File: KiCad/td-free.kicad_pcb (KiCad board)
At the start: 2 copper layers, 60 x 30 mm, 6 parts, among them J1 Conn_01x02_Pin, Q1 2N7002, U1 ESP32-C3_SUPERMINI, U2 VEML7700-TT

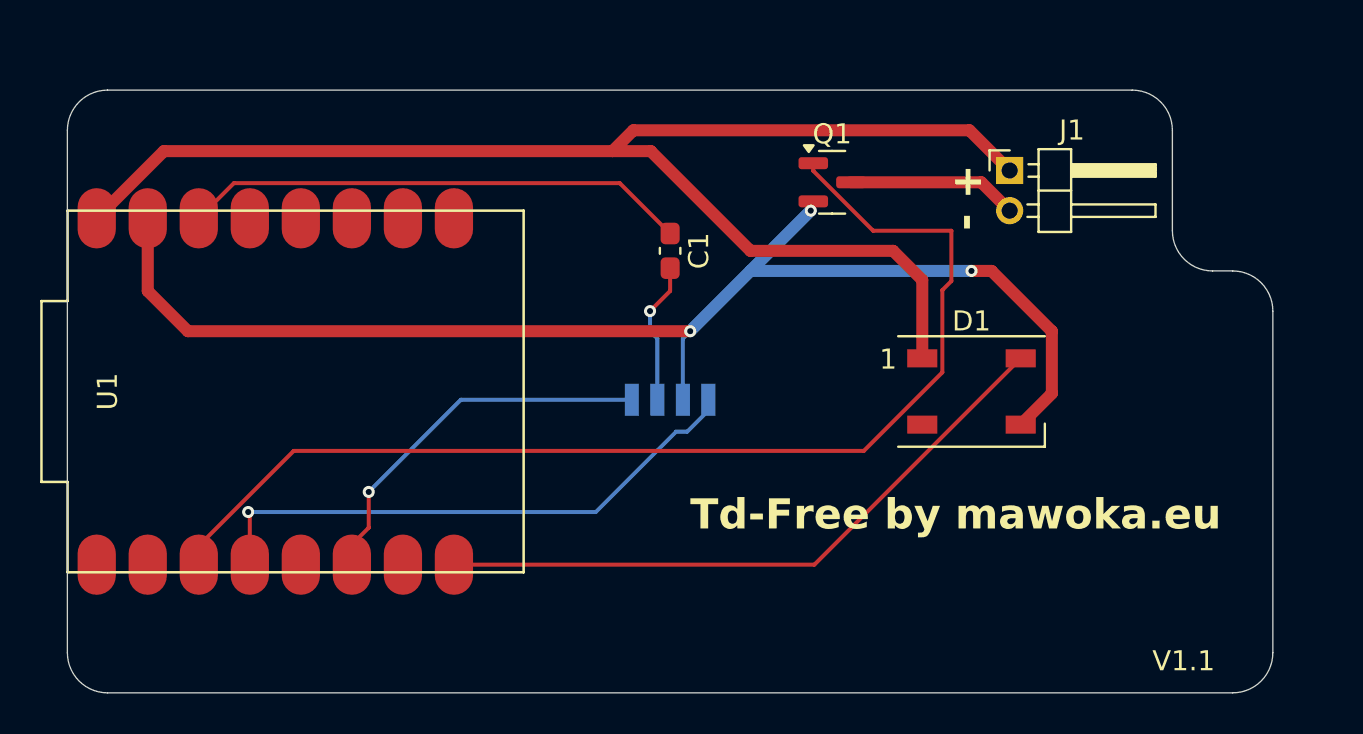
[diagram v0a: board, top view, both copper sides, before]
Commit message: Add V1.2 PCB without wrong condensator
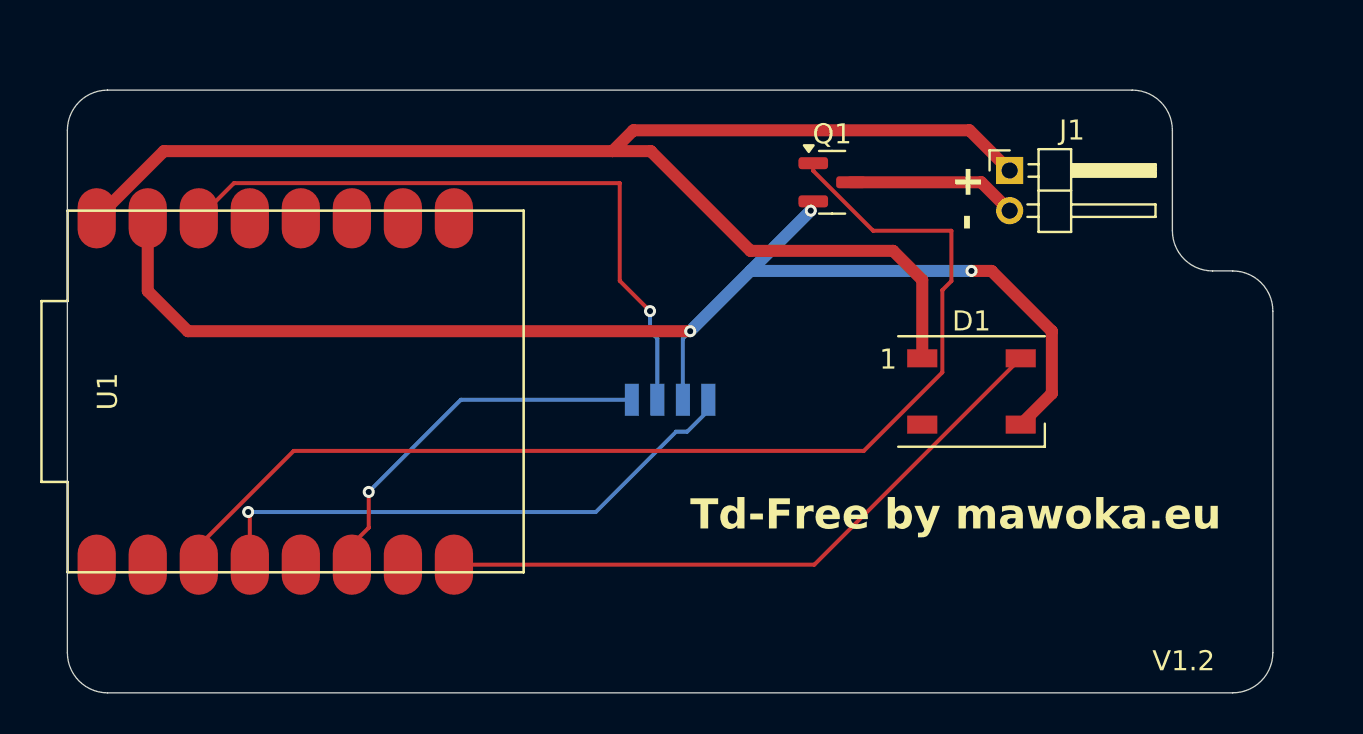
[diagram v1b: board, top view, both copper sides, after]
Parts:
- removed C1: C_Small, Capacitor_SMD:C_0603_1608Metric_Pad1.08x0.95mm_HandSolder
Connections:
- U2 pad 2: Net-(U2-VDD) -> Net-(U1-3V3)
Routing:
- net Net-(U1-3V3): track 25.2 -> 32.7 mm, vias 0 -> 1
- net Net-(U2-VDD): track 6.62 -> 0.00 mm, vias 1 -> 0
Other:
- board text added: "V1.2"
- board text removed: "V1.1"

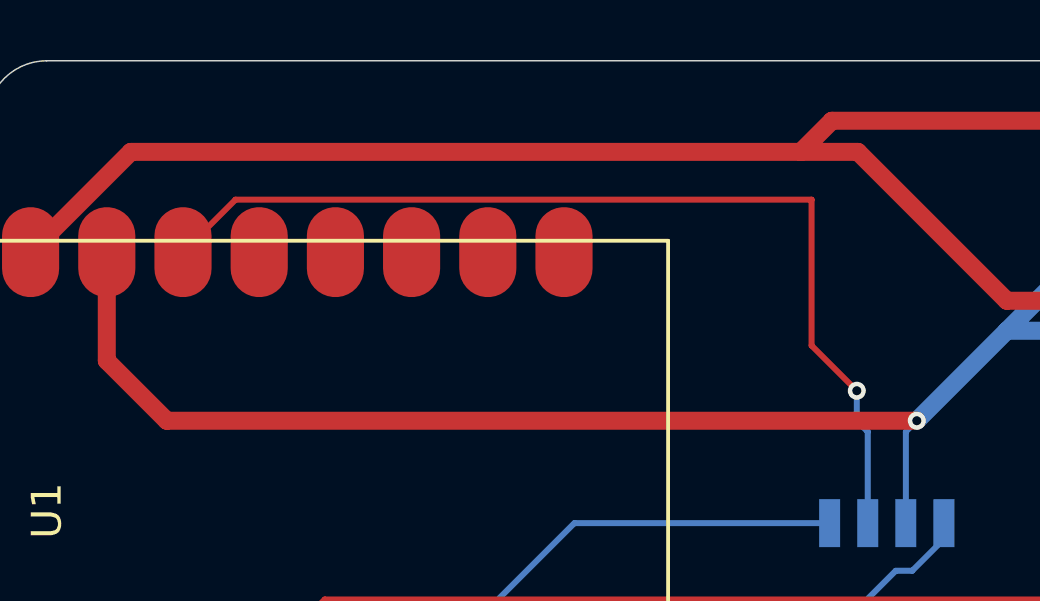
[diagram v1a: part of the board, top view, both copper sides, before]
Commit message: Optimize trace on PCB
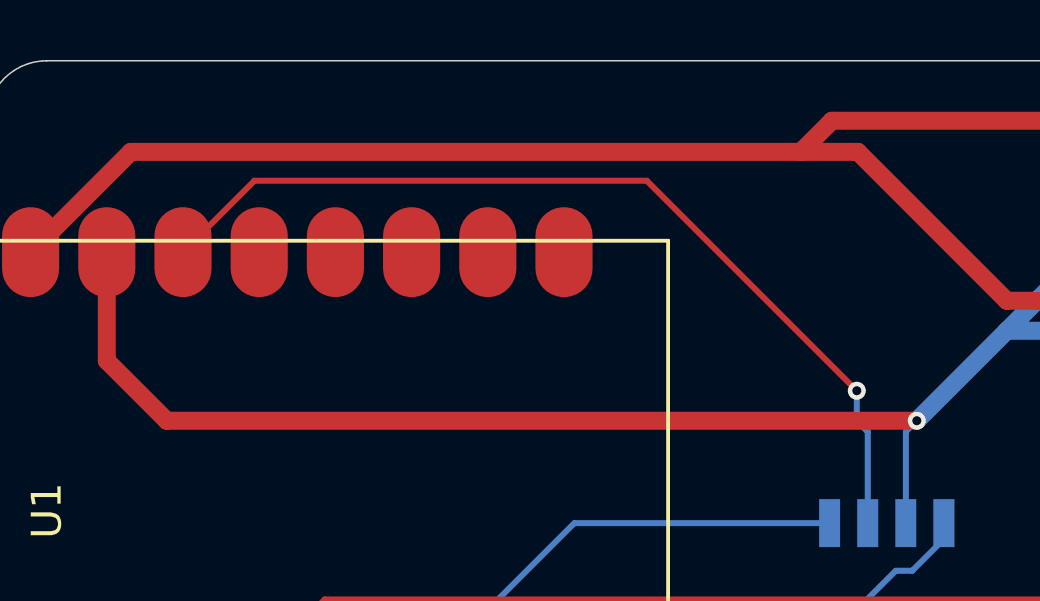
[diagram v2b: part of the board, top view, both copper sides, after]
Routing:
- net Net-(U1-3V3): track 32.7 -> 30.4 mm
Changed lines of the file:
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@@
 	)
 	(segment
-		(start 41.4925 19.63)
-		(end 41.4925 24.4925)
+		(start 22.92 19)
+		(end 20.54 21.38)
 		(width 0.2)
 		(layer "F.Cu")
@@
 	)
 	(segment
-		(start 22.29 19.63)
-		(end 41.4925 19.63)
+		(start 43 26)
+		(end 36 19)
 		(width 0.2)
 		(layer "F.Cu")
@@
 	)
 	(segment
-		(start 41.4925 24.4925)
-		(end 43 26)
+		(start 36 19)
+		(end 22.92 19)
 		(width 0.2)
 		(layer "F.Cu")
-		(net 5)
-	)
-	(segment
-		(start 20.54 21.38)
-		(end 22.29 19.63)
-		(width 0.2)
-		(layer "F.Cu")

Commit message: :sparkles: First Prototype for improved PCB
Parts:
- added C1: 10uF, Capacitor_SMD:C_0805_2012Metric_Pad1.18x1.45mm_HandSolder, F.Cu at (21.0, 19.0)
- added C2: 22uF, Capacitor_SMD:C_0805_2012Metric_Pad1.18x1.45mm_HandSolder, F.Cu at (37.0, 19.0)
- added C3: 22uF, Capacitor_SMD:C_0805_2012Metric_Pad1.18x1.45mm_HandSolder, F.Cu at (38.0, 26.0)
- added C4: 10uF, Capacitor_SMD:C_0805_2012Metric_Pad1.18x1.45mm_HandSolder, F.Cu at (48.0, 28.0)
- added C5: 0.1uF, Capacitor_SMD:C_0805_2012Metric_Pad1.18x1.45mm_HandSolder, F.Cu at (48.0, 24.0)
- added C6: 10uF, Capacitor_SMD:C_0805_2012Metric_Pad1.18x1.45mm_HandSolder, F.Cu at (38.0, 31.0)
- added D2: SMAJ5.0A, Diode_SMD:D_SMA, F.Cu at (19.0, 38.0)
- added J2: USB_C_Receptacle_USB2.0_14P, Connector_USB:USB_C_Receptacle_GCT_USB4105-xx-A_16P_TopMnt_Horizontal, F.Cu at (18.2, 30.0)
- added R1: 5k1, Resistor_SMD:R_0805_2012Metric_Pad1.20x1.40mm_HandSolder, F.Cu at (22.0, 22.0)
- added R2: 5k1, Resistor_SMD:R_0805_2012Metric_Pad1.20x1.40mm_HandSolder, F.Cu at (18.0, 22.0)
- added R3: 10kO, Resistor_SMD:R_0805_2012Metric_Pad1.20x1.40mm_HandSolder, F.Cu at (50.0, 40.0)
- added U3: AMS1117-3.3, Package_TO_SOT_SMD:SOT-223-3_TabPin2, F.Cu at (29.1, 20.7)
- added U4: VEML3328, footprints:SMD_L3328_VIS, F.Cu at (44.0, 32.7)
- added U5: TPD4E05U06DQA, Package_SON:USON-10_2.5x1.0mm_P0.5mm, F.Cu at (25.4, 35.0)
- J1: footprint Connector_PinHeader_2.00mm:PinHeader_1x02_P2.00mm_Horizontal -> Connector_PinHeader_2.54mm:PinHeader_1x02_P2.54mm_Vertical
- U1: value ESP32-C3_SUPERMINI -> ESP32-C3-WROOM-02; footprint ESP32-C3_SUPERMINI:MODULE_ESP32-C3_SUPERMINI -> PCM_Espressif:ESP32-C3-WROOM-02
- U2: footprint VEML7700-TT:XDCR_VEML7700-TT -> VEML7700_TR:XDCR_VEML7700-TR; moved to F.Cu
- moved U1 33.6 mm to (58.9, 28.3), turned to 0 degrees
- moved D1 28.0 mm to (31.0, 30.0)
- moved Q1 21.8 mm to (55.9, 41.0)
- moved J1 12.9 mm to (71.0, 27.0)
- moved U2 5.32 mm to (44.3, 26.0), turned to 0 degrees
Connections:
- net Net-(U1-GPIO10) renamed /SCL
- D1 pad 1: Net-(D1-VDD) -> VBUS
- D1 pad 3: Net-(D1-VSS) -> GND
- D1 pad 4: Net-(D1-DIN) -> /RGB_DATA
- J1 pad 1: Net-(D1-VDD) -> VBUS
- Q1 pad 1: Net-(Q1-G) -> /LED_C
- Q1 pad 2: Net-(D1-VSS) -> GND
- U1 pad 1: unconnected-(U1-GPIO1-Pad1) -> +3V3
- U1 pad 2: unconnected-(U1-GPIO2-Pad2) -> Net-(U1-EN/CHIP_PU)
- U1 pad 6: unconnected-(U1-GPIO6-Pad6) -> /LED_C
- U1 pad 7: Net-(Q1-G) -> /SDA
- U1 pad 8: Net-(U1-GPIO8) -> /RGB_DATA
- U1 pad 9: unconnected-(U1-GPIO9-Pad9) -> GND
- U2 pad 2: Net-(U1-3V3) -> +3V3
- U2 pad 3: Net-(D1-VSS) -> GND
- U2 pad 4: Net-(U1-GPIO8) -> /SDA
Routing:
- net VBUS: track 0.00 -> 108.5 mm
- net Net-(D1-VDD): track 70.1 -> 0.00 mm
- net Net-(D1-VSS): track 64.0 -> 0.00 mm, vias 3 -> 0
- net /USB_D+: track 0.00 -> 57.9 mm, vias 0 -> 2
- net Net-(Q1-G): track 57.3 -> 0.00 mm
- net +3V3: track 0.00 -> 55.8 mm
- net /USB_D-: track 0.00 -> 55.8 mm, vias 0 -> 3
- net Net-(D1-DIN): track 32.5 -> 0.00 mm
- net Net-(U1-3V3): track 30.4 -> 0.00 mm, vias 1 -> 0
- net Net-(U1-GPIO8): track 27.2 -> 0.00 mm, vias 1 -> 0
- net GND: track 0.00 -> 24.8 mm, vias 0 -> 30
- net /RGB_DATA: track 0.00 -> 18.8 mm, vias 0 -> 2
- net /SCL: track 18.0 -> 36.6 mm, vias 1 -> 3
- net Net-(U1-EN/CHIP_PU): track 0.00 -> 18.3 mm
- net Net-(J1-Pin_2): track 8.49 -> 21.4 mm
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- added copper zone on B.Cu, net GND
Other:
- outline, holes or cut-outs redrawn
- board text added: "V2.0"
- board text removed: "- +"
- board text removed: "V1.2"

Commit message: :sparkles: First test with new PCB
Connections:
- U1 pad 10: /SCL -> /SCL1
- U1 pad 4: unconnected-(U1-GPIO5/ADC2_CH0-Pad4) -> /SCL2
- U1 pad 5: unconnected-(U1-GPIO6-Pad5) -> /SDA2
- U1 pad 7: /SDA -> /SDA1
- U2 pad 1: /SCL -> /SCL2
- U2 pad 4: /SDA -> /SDA2
- U4 pad 2: /SDA -> /SDA1
- U4 pad 3: /SCL -> /SCL1
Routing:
- net /SCL: track 36.6 -> 0.00 mm, vias 3 -> 0
- net /SCL1: track 0.00 -> 24.2 mm, vias 0 -> 2
- net /SDA: track 12.0 -> 0.00 mm, vias 2 -> 0
- net /SDA1: track 0.00 -> 7.86 mm, vias 0 -> 2
- net /SCL2: track 0.00 -> 6.39 mm, vias 0 -> 2
- net /SDA2: track 0.00 -> 5.40 mm
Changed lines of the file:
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@@
 	(title_block
 		(title "Td-Free")
-		(rev "0")
+		(rev "1")
 		(comment 4 "AISLER Project ID: AKNQHGTF")
 	)
@@
 	(net 13 "unconnected-(U1-GPIO20{slash}U0RXD-Pad11)")
 	(net 14 "unconnected-(U1-GPIO2{slash}ADC1_CH2-Pad16)")
-	(net 15 "unconnected-(U1-GPIO5{slash}ADC2_CH0-Pad4)")
+	(net 15 "/SCL2")
 	(net 16 "unconnected-(U1-GPIO0{slash}ADC1_CH0{slash}XTAL_32K_P-Pad18)")
 	(net 17 "unconnected-(U1-GPIO4{slash}ADC1_CH4-Pad3)")
 	(net 18 "unconnected-(U1-GPIO1{slash}ADC1_CH1{slash}XTAL_32K_N-Pad17)")
 	(net 19 "unconnected-(U1-GPIO3{slash}ADC1_CH3-Pad15)")
-	(net 20 "unconnected-(U1-GPIO6-Pad5)")
+	(net 20 "/SDA2")
 	(net 21 "unconnected-(U1-GPIO21{slash}U0TXD-Pad12)")
-	(net 22 "/SCL")
-	(net 23 "/SDA")
+	(net 22 "/SCL1")
+	(net 23 "/SDA1")
 	(net 24 "unconnected-(U5-NC-Pad10)")
 	(net 25 "unconnected-(U5-NC-Pad6)")
@@
 			(size 1.5 0.9)
 			(layers "F.Cu" "F.Mask" "F.Paste")
-			(net 15 "unconnected-(U1-GPIO5{slash}ADC2_CH0-Pad4)")
+			(net 15 "/SCL2")
 			(pinfunction "GPIO5/ADC2_CH0")
-			(pintype "bidirectional+no_connect")
+			(pintype "bidirectional")
 		)
 		(pad "5" smd rect
@@
 			(size 1.5 0.9)
 			(layers "F.Cu" "F.Mask" "F.Paste")
-			(net 20 "unconnected-(U1-GPIO6-Pad5)")
+			(net 20 "/SDA2")
 			(pinfunction "GPIO6")
-			(pintype "bidirectional+no_connect")
+			(pintype "bidirectional")
 		)
 		(pad "6" smd rect
@@
 			(size 1.5 0.9)
 			(layers "F.Cu" "F.Mask" "F.Paste")
-			(net 23 "/SDA")
+			(net 23 "/SDA1")
 			(pinfunction "GPIO8")
 			(pintype "bidirectional")
@@
 			(size 1.5 0.9)
 			(layers "F.Cu" "F.Mask" "F.Paste")
-			(net 22 "/SCL")
+			(net 22 "/SCL1")
 			(pinfunction "GPIO10")
 			(pintype "bidirectional")
@@
 			(size 1.4 0.7)
 			(layers "F.Cu" "F.Mask" "F.Paste")
-			(net 22 "/SCL")
+			(net 15 "/SCL2")
 			(pinfunction "SCL")
 			(pintype "input")
@@
 			(size 1.4 0.7)
 			(layers "F.Cu" "F.Mask" "F.Paste")
-			(net 23 "/SDA")
+			(net 20 "/SDA2")
 			(pinfunction "SDA")
 			(pintype "bidirectional")
@@
 			(size 0.4318 0.3048)
 			(layers "F.Cu" "F.Mask" "F.Paste")
-			(net 23 "/SDA")
+			(net 23 "/SDA1")
 			(pinfunction "SDA")
 			(pintype "bidirectional")
@@
 			(size 0.5334 0.3556)
 			(layers "F.Cu" "F.Mask" "F.Paste")
-			(net 22 "/SCL")
+			(net 22 "/SCL1")
 			(pinfunction "SCL")
 			(pintype "input")
@@
 	)
 	(segment
-		(start 52.4 34.4)
-		(end 67.69 34.4)
+		(start 45.881838 24.095)
+		(end 45.988419 23.988419)
 		(width 0.2)
 		(layer "F.Cu")
-		(net 22)
+		(net 15)
 	)
 	(segment
@@
 		(width 0.2)
 		(layer "F.Cu")
+		(net 15)
+	)
+	(segment
+		(start 45 24.095)
+		(end 45.881838 24.095)
+		(width 0.2)
+		(layer "F.Cu")
+		(net 15)
+	)
+	(via
+		(at 50 27)
+		(size 0.6)
+		(drill 0.3)
+		(layers "F.Cu" "B.Cu")
+		(net 15)
+	)
+	(via
+		(at 45.988419 23.988419)
+		(size 0.6)
+		(drill 0.3)
+		(layers "F.Cu" "B.Cu")
+		(net 15)
+	)
+	(segment
+		(start 45.988419 23.988419)
+		(end 49 27)
+		(width 0.2)
+		(layer "B.Cu")
+		(net 15)
+	)
+	(segment
+		(start 49 27)
+		(end 50 27)
+		(width 0.2)
+		(layer "B.Cu")
+		(net 15)
+	)
+	(segment
+		(start 49.695 27.905)
+		(end 50.19 28.4)
+		(width 0.2)
+		(layer "F.Cu")
+		(net 20)
+	)
+	(segment
+		(start 45 27.905)
+		(end 49.695 27.905)
+		(width 0.2)
+		(layer "F.Cu")
+		(net 20)
+	)
+	(segment
+		(start 52.4 34.4)
+		(end 67.69 34.4)
+		(width 0.2)
+		(layer "F.Cu")
 		(net 22)
 	)
@@
 	)
 	(via
-		(at 45 24)
-		(size 0.6)
-		(drill 0.3)
-		(layers "F.Cu" "B.Cu")
-		(net 22)
-	)
-	(via
 		(at 52 34)
 		(size 0.6)
@@
 	)
 	(segment
-		(start 45 34)
-		(end 48.5 30.5)
-		(width 0.2)
-		(layer "B.Cu")
-		(net 22)
-	)
-	(segment
-		(start 48 30)
-		(end 48.5 30.5)
-		(width 0.2)
-		(layer "B.Cu")
-		(net 22)
-	)
-	(segment
-		(start 48.5 30.5)
-		(end 52 34)
+		(start 45.361 33.639)
+		(end 45 34)
 		(width 0.2)
 		(layer "B.Cu")
@@
 	)
 	(segment
-		(start 45 30)
-		(end 48 30)
+		(start 52 34)
+		(end 51.639 33.639)
 		(width 0.2)
 		(layer "B.Cu")
@@
 	)
 	(segment
-		(start 45 24)
-		(end 45 30)
+		(start 51.639 33.639)
+		(end 45.361 33.639)
 		(width 0.2)
 		(layer "B.Cu")
@@
 	)
 	(segment
-		(start 43.334979 33)
-		(end 43.824657 32.510322)
-		(width 0.2)
-		(layer "F.Cu")
-		(net 23)
-	)
-	(segment
 		(start 43.162501 33)
 		(end 43.334979 33)
@@
 	)
 	(segment
-		(start 48.495 31.4)
-		(end 50.19 31.4)
+		(start 50.19 31.4)
+		(end 47.6 31.4)
 		(width 0.2)
 		(layer "F.Cu")
@@
 	)
 	(segment
-		(start 45 27.905)
-		(end 48.495 31.4)
+		(start 47.6 31.4)
+		(end 47 32)
 		(width 0.2)
 		(layer "F.Cu")
@@
 	)
 	(via
-		(at 43.824657 32.510322)
+		(at 43.162501 33)
 		(size 0.6)
 		(drill 0.3)
@@
 	)
 	(via
-		(at 44.45 28.256)
+		(at 47 32)
 		(size 0.6)
 		(drill 0.3)
@@
 	)
 	(segment
-		(start 44 28.706)
-		(end 44.45 28.256)
-		(width 0.2)
-		(layer "B.Cu")
-		(net 23)
-	)
-	(segment
-		(start 43.824657 32.510322)
-		(end 44 32.334979)
+		(start 47 32)
+		(end 46 33)
 		(width 0.2)
 		(layer "B.Cu")
@@
 	)
 	(segment
-		(start 44 32.334979)
-		(end 44 28.706)
+		(start 46 33)
+		(end 43.162501 33)
 		(width 0.2)
 		(layer "B.Cu")

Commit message: :sparkles: PCB Progress
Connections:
- U1 pad 3: unconnected-(U1-GPIO4/ADC1_CH4-Pad3) -> /RGB_DATA
- U1 pad 8: /RGB_DATA -> unconnected-(U1-GPIO9-Pad8)
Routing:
- net /RGB_DATA: track 18.8 -> 19.7 mm
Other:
- board text added: "V2.1"
- board text removed: "V2.0"
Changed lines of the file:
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@@
 	(net 15 "/SCL2")
 	(net 16 "unconnected-(U1-GPIO0{slash}ADC1_CH0{slash}XTAL_32K_P-Pad18)")
-	(net 17 "unconnected-(U1-GPIO4{slash}ADC1_CH4-Pad3)")
+	(net 17 "unconnected-(U1-GPIO9-Pad8)")
 	(net 18 "unconnected-(U1-GPIO1{slash}ADC1_CH1{slash}XTAL_32K_N-Pad17)")
 	(net 19 "unconnected-(U1-GPIO3{slash}ADC1_CH3-Pad15)")
@@
 		)
 		(embedded_fonts no)
-		(model "${KICAD8_3DMODEL_DIR}/Connector_PinHeader_2.54mm.3dshapes/PinHeader_1x02_P2.54mm_Vertical.wrl"
-			(offset
-				(xyz 0 0 0)
-			)
-			(scale
-				(xyz 1 1 1)
-			)
-			(rotate
-				(xyz 0 0 0)
-			)
-		)
 	)
 	(footprint "Resistor_SMD:R_0805_2012Metric_Pad1.20x1.40mm_HandSolder"
@@
 			(size 1.5 0.9)
 			(layers "F.Cu" "F.Mask" "F.Paste")
-			(net 17 "unconnected-(U1-GPIO4{slash}ADC1_CH4-Pad3)")
+			(net 6 "/RGB_DATA")
 			(pinfunction "GPIO4/ADC1_CH4")
-			(pintype "bidirectional+no_connect")
+			(pintype "bidirectional")
 		)
 		(pad "4" smd rect
@@
 			(size 1.5 0.9)
 			(layers "F.Cu" "F.Mask" "F.Paste")
-			(net 6 "/RGB_DATA")
+			(net 17 "unconnected-(U1-GPIO9-Pad8)")
 			(pinfunction "GPIO9")
-			(pintype "bidirectional")
+			(pintype "bidirectional+no_connect")
 		)
 		(pad "9" smd rect
@@
 		)
 		(embedded_fonts no)
+		(model "/home/mawoka/Documents/KiCad/Library/VEML7700_TR/VEML7700-TR.step"
+			(offset
+				(xyz 0 0 1)
+			)
+			(scale
+				(xyz 1 1 1)
+			)
+			(rotate
+				(xyz -90 -0 -0)
+			)
+		)
 	)
 	(footprint "Connector_USB:USB_C_Receptacle_GCT_USB4105-xx-A_16P_TopMnt_Horizontal"
@@
 		)
 		(embedded_fonts no)
+		(model "/home/mawoka/Documents/KiCad/Library/VEML3328/80216oplga4l.stp"
+			(offset
+				(xyz 0 0 0)
+			)
+			(scale
+				(xyz 1 1 1)
+			)
+			(rotate
+				(xyz 0 0 0)
+			)
+		)
 	)
 	(footprint "Capacitor_SMD:C_0805_2012Metric_Pad1.18x1.45mm_HandSolder"
@@
 		(layer "Edge.Cuts")
 	)
-	(gr_text "V2.0\n"
+	(gr_text "V2.1\n"
 		(at 68 42 0)
 		(layer "F.SilkS")
@@
 	)
 	(segment
-		(start 43.217829 29.782171)
-		(end 43.782171 29.782171)
-		(width 0.2)
-		(layer "F.Cu")
-		(net 6)
-	)
-	(segment
-		(start 43.782171 29.782171)
-		(end 46.9 32.9)
-		(width 0.2)
-		(layer "F.Cu")
-		(net 6)
-	)
-	(segment
 		(start 33.45 28.35)
-		(end 39.35 28.35)
+		(end 39.65 28.35)
 		(width 0.2)
 		(layer "F.Cu")
@@
 	)
 	(segment
-		(start 46.9 32.9)
-		(end 50.19 32.9)
-		(width 0.2)
-		(layer "F.Cu")
-		(net 6)
-	)
-	(segment
-		(start 39.35 28.35)
-		(end 39.988419 28.988419)
+		(start 39.65 28.35)
+		(end 40 28)
 		(width 0.2)
 		(layer "F.Cu")
@@
 	)
 	(via
-		(at 43.217829 29.782171)
+		(at 40 28)
 		(size 0.6)
 		(drill 0.3)
@@
 	)
 	(via
-		(at 39.988419 28.988419)
+		(at 50.19 25.4)
 		(size 0.6)
 		(drill 0.3)
@@
 	)
 	(segment
-		(start 43.217829 29.782171)
-		(end 43 30)
+		(start 40 28)
+		(end 49.779232 28)
+		(width 0.2)
+		(layer "B.Cu")
+		(net 6)
+	)
+	(segment
+		(start 49.779232 28)
+		(end 50.79 26.989232)
 		(width 0.2)
 		(layer "B.Cu")
@@
 	)
 	(segment
-		(start 43 30)
-		(end 41 30)
+		(start 50.79 26.989232)
+		(end 50.79 26)
 		(width 0.2)
 		(layer "B.Cu")
@@
 	)
 	(segment
-		(start 41 30)
-		(end 39.988419 28.988419)
+		(start 50.79 26)
+		(end 50.19 25.4)
 		(width 0.2)
 		(layer "B.Cu")
